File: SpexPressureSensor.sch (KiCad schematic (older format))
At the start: 31 parts, among them J1 3PinJumper, P1 CONN_6, P2 NICHROME, P3 TC2030-CTX, Q1 IRLL3303PbF, U1 ST1480ABDR, U2 TPS769XX, U3 MKL03ZxxVFG4, U4 BMP180, U5 MMA8653FC

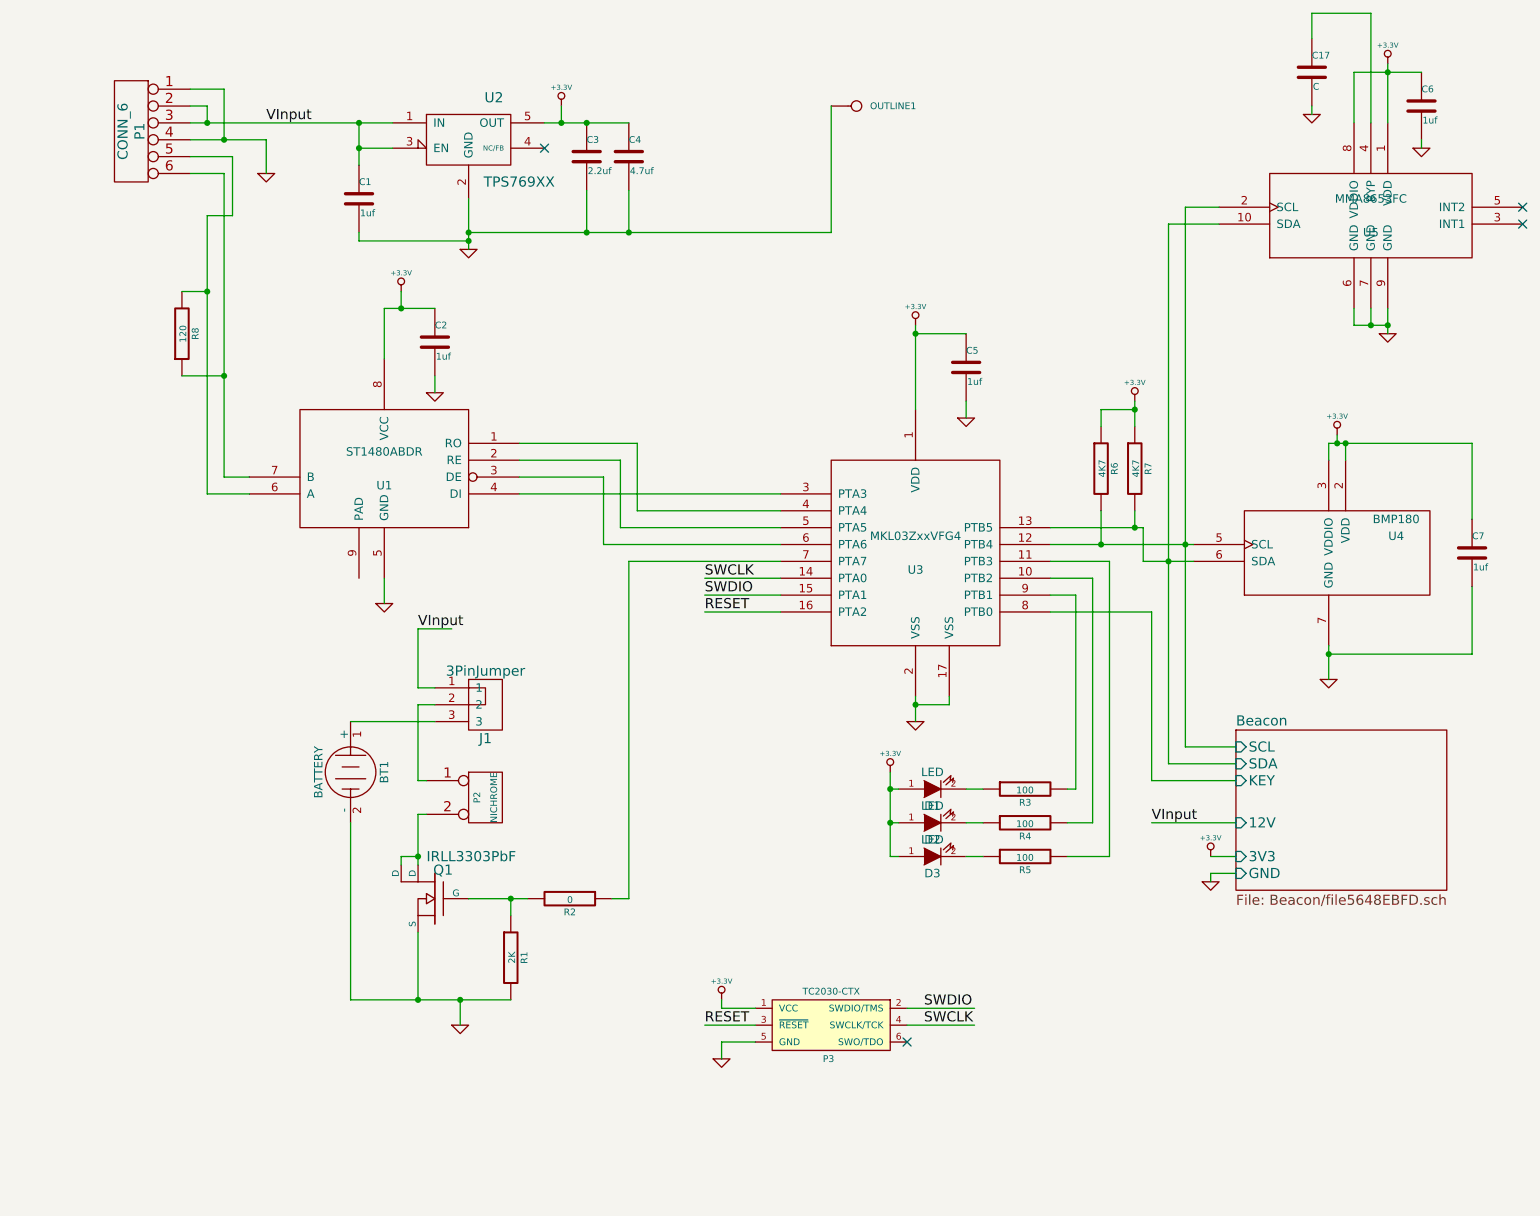
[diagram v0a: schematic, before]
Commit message: Added a current monitor on the nichrome.
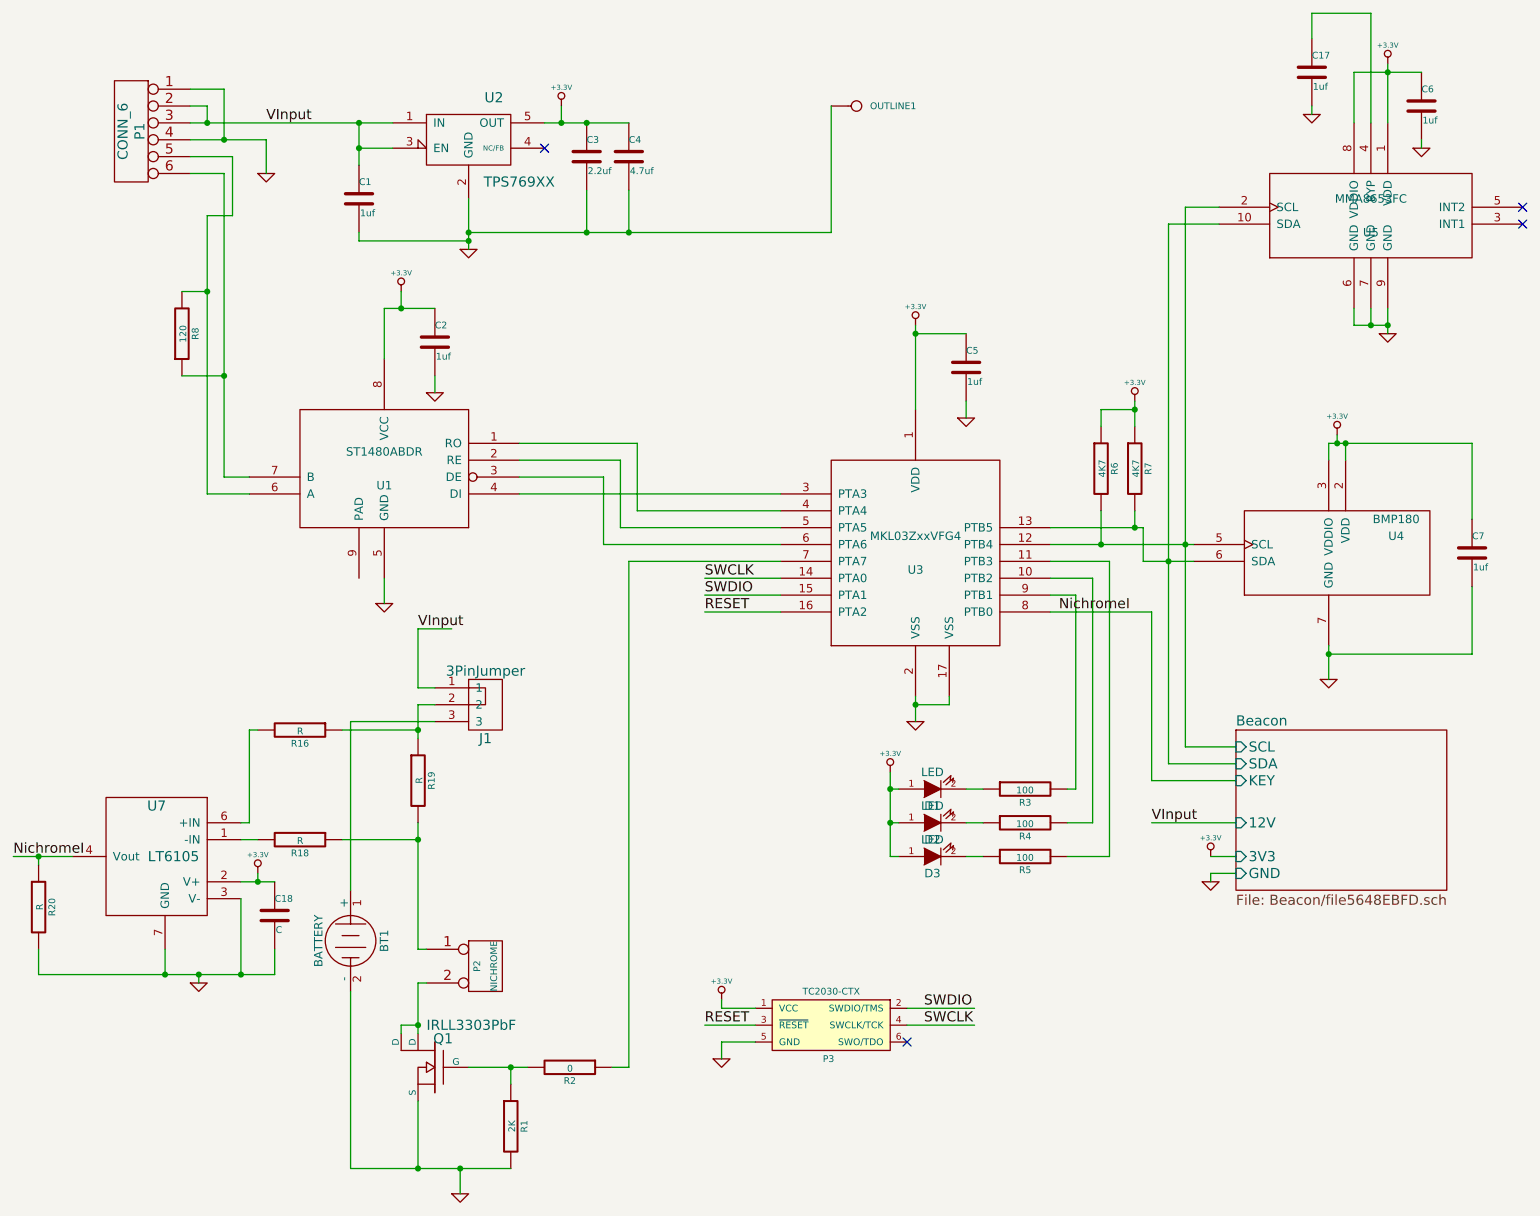
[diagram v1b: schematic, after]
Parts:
- added C18: C, Capacitors_SMD:C_0402, symbol C
- added R16, R18, R20: R, Resistors_SMD:R_0402, symbol R
- added R19: R, Resistors_SMD:R_0805, symbol R
- added U7: LT6105, LT6105:LT6105, symbol LT6105
- C17: value C -> 1uf
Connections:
- net +3.3V: now also C18.1, U7.2 (V+)
- net GND: now also C18.2, R20.2, U7.3 (V-), U7.7 (GND)
- net at P2.1 (P1): now also R18.1, R19.2; no longer J1.2
- net Beacon/KEY renamed NichromeI
- net NichromeI: now also R20.1, U7.4 (Vout)
- new net: J1.2, R16.1, R19.1
- new net: R16.2, U7.6 (+IN)
- new net: R18.2, U7.1 (-IN)
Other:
- moved on the sheet: BT1, P2, Q1, R1, R2

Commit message: Realized the board was tooooo big.
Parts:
- removed BT1: BATTERY, Pin_Headers:Pin_Header_Straight_1x02, symbol BATTERY
- removed C17, C6: 1uf, Capacitors_SMD:C_0402, symbol C
- removed D2, D3: LED, LEDs:LED-0603, symbol LED
- removed J1: 3PinJumper, solderJmp:3solderJmp, symbol 3PinJumper
- removed R4, R5: 100, Resistors_SMD:R_0402, symbol R
- removed U5: MMA8653FC, MMA8653FC:MMA8653FCR1, symbol MMA8653FC
- U1: footprint Housings_SOIC:SOIC-8_3.9x4.9mm_Pitch1.27mm -> Housings_DFN_QFN:DFN-8-1EP_3x3mm_Pitch0.5mm; Manufacturer PN (none) -> LTC2851IDD
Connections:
- wire segments 155 -> 117
- no-connect marks 4 -> 2

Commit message: Finished board. Ready to go. Should add gerbers.
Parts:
- C1, C18, C2, C3, C4, C5, C7: symbol C -> C-RESCUE-SpexPressureSensor
- D1: symbol LED -> LED-RESCUE-SpexPressureSensor
- R1, R16, R18, R19, R2, R20, R3, R6, R7, R8: symbol R -> R-RESCUE-SpexPressureSensor
- U2: symbol TPS769XX -> TPS769XX-RESCUE-SpexPressureSensor
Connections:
- net labels added: cut
- wire segments 117 -> 116
